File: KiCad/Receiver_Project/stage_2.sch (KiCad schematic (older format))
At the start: 14 parts, among them Q5 2N3904, Q6 2N3904, Q7 PN2369A, Q8 2N3904, Q9 PN2369A

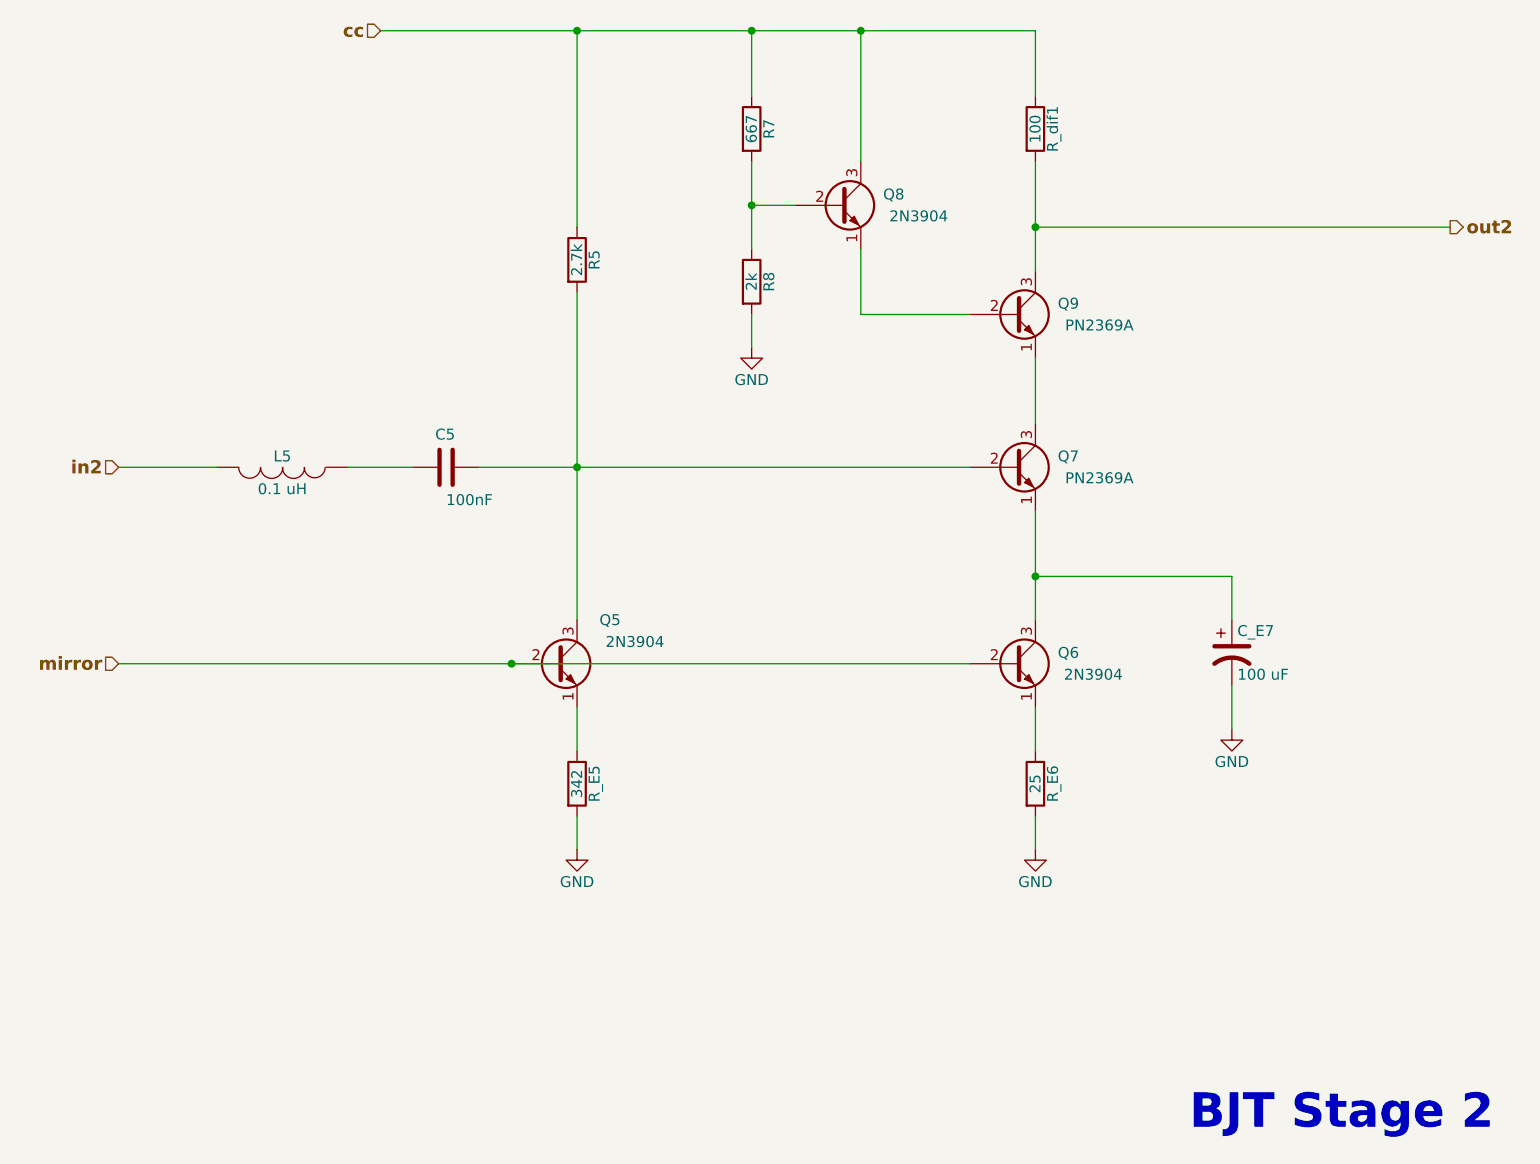
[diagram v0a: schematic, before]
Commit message: added simulation labels to receiver schematic
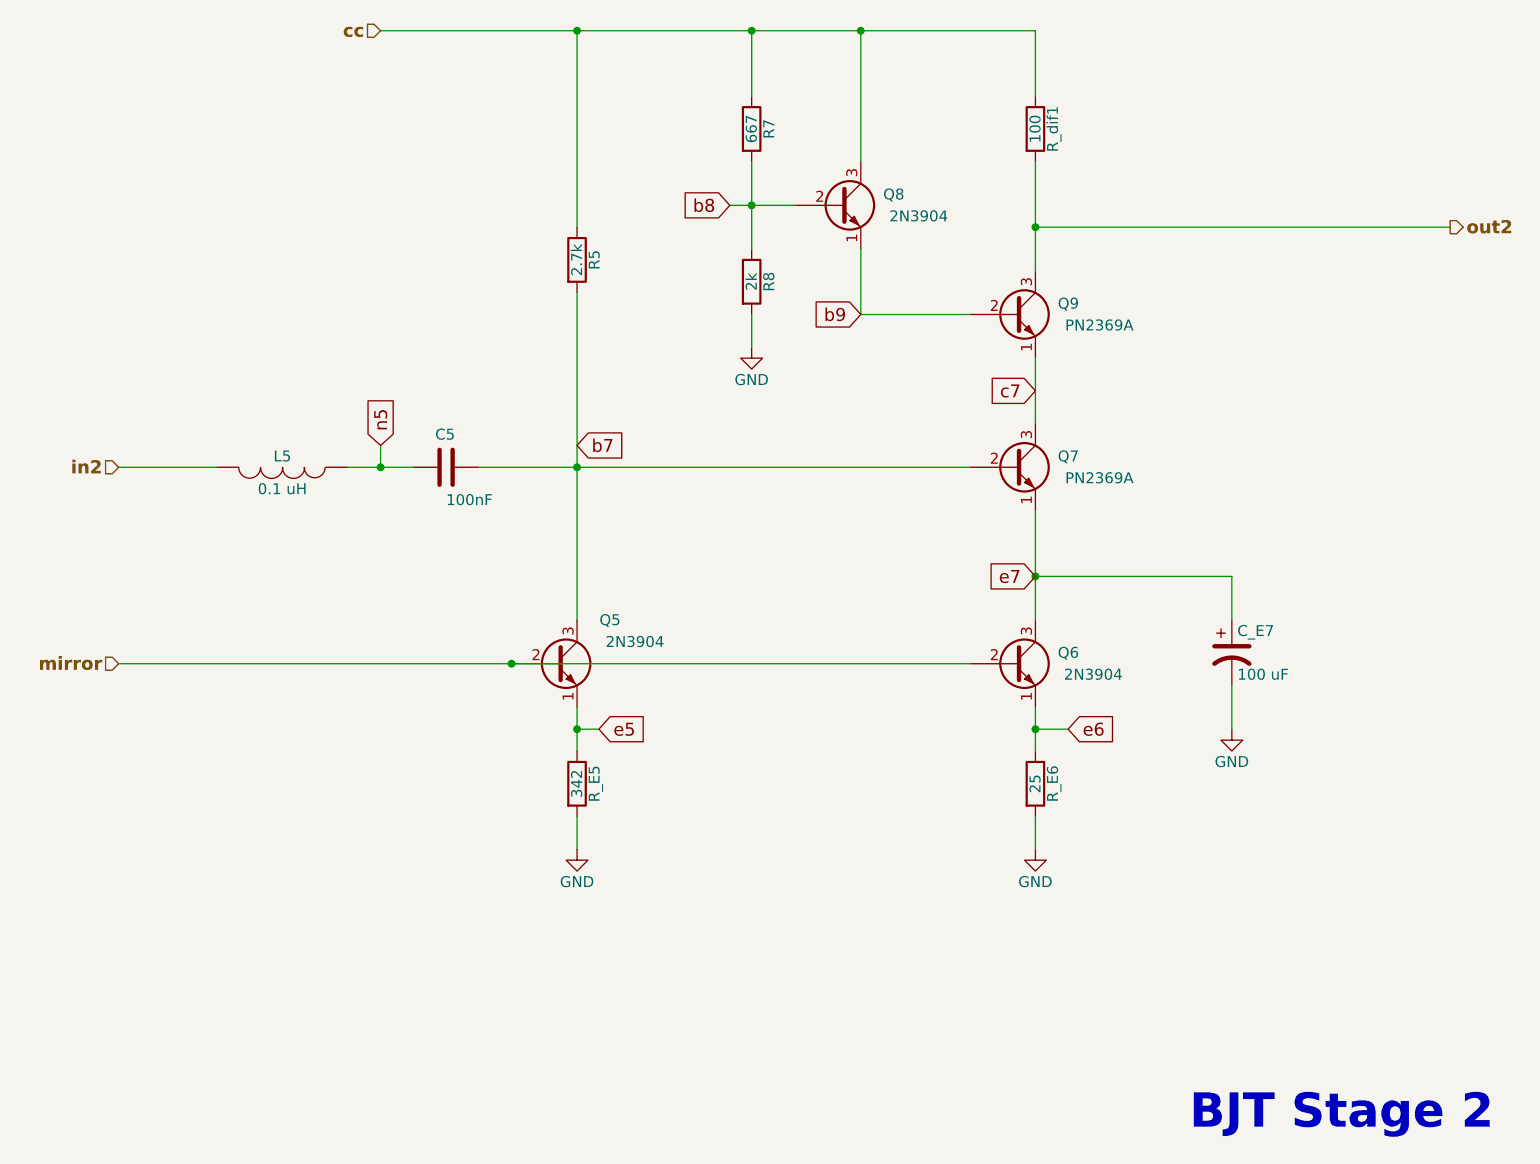
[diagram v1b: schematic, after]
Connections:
- net n5: now reaches C5.2, L5.1
- net b7: now reaches C5.1, Q5.3 (C), Q7.2 (B), R5.2
- net e5: now reaches Q5.1 (E), R_E5.1
- net e6: now reaches Q6.1 (E), R_E6.1
- net e7: now reaches C_E7.1, Q6.3 (C), Q7.1 (E)
- net b9: now reaches Q8.1 (E), Q9.2 (B)
- net b8: now reaches Q8.2 (B), R7.2, R8.1
- net c7: now reaches Q7.3 (C), Q9.1 (E)
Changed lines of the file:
@@
 	5300 2500 5300 2900
 Wire Wire Line
-	5500 2700 5300 2700
+	5200 2700 5500 2700
 Connection ~ 5300 2700
 Wire Wire Line
@@
 	4500 3100 4500 4600
 Connection ~ 4500 3900
+Text GLabel 3600 3800 1    59   Input ~ 0
+n5
+Wire Wire Line
+	3600 3800 3600 3900
+Connection ~ 3600 3900
+Text GLabel 4500 3800 2    59   Input ~ 0
+b7
+Text GLabel 4600 5100 2    59   Input ~ 0
+e5
+Wire Wire Line
+	4600 5100 4500 5100
+Connection ~ 4500 5100
+Wire Wire Line
+	6600 5100 6750 5100
+Connection ~ 6600 5100
+Text GLabel 6750 5100 2    59   Input ~ 0
+e6
+Text GLabel 6600 4400 0    59   Input ~ 0
+e7
+Text GLabel 6600 3550 0    59   Input ~ 0
+c7
+Text GLabel 5800 3200 0    59   Input ~ 0
+b9
+Text GLabel 5200 2700 0    59   Input ~ 0
+b8
 $EndSCHEMATC
